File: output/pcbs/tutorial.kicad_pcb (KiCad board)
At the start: 2 copper layers, 379.6 x 123.2 mm, 184 parts

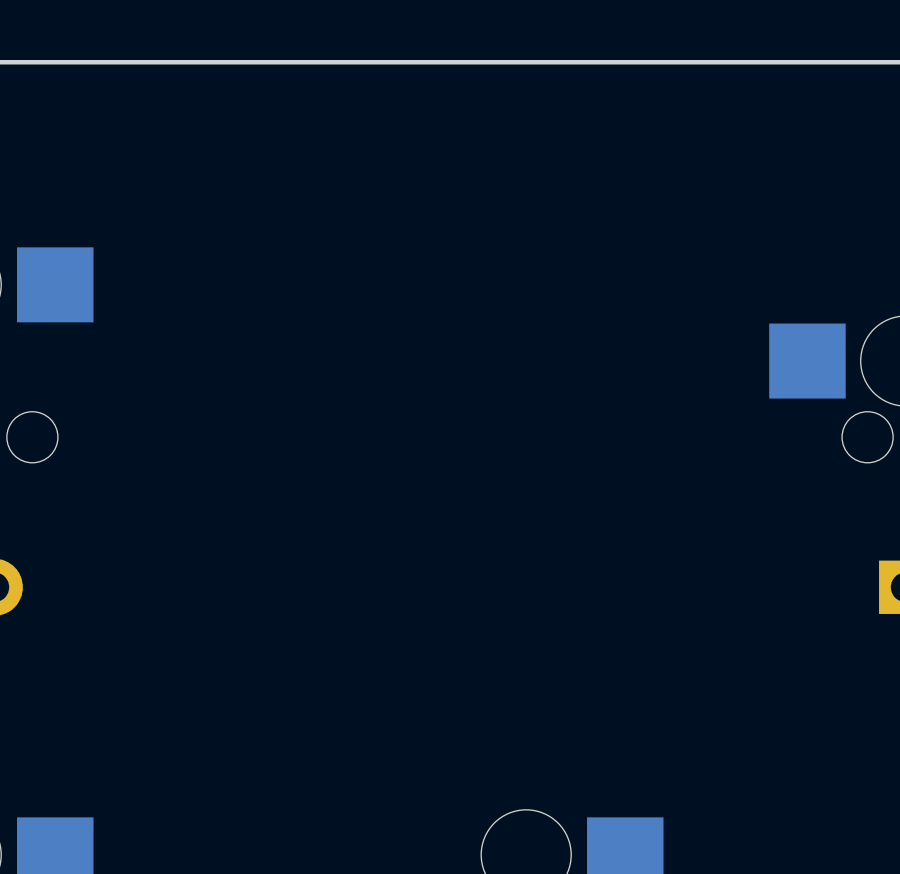
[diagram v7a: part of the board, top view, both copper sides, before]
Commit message: added dip-16
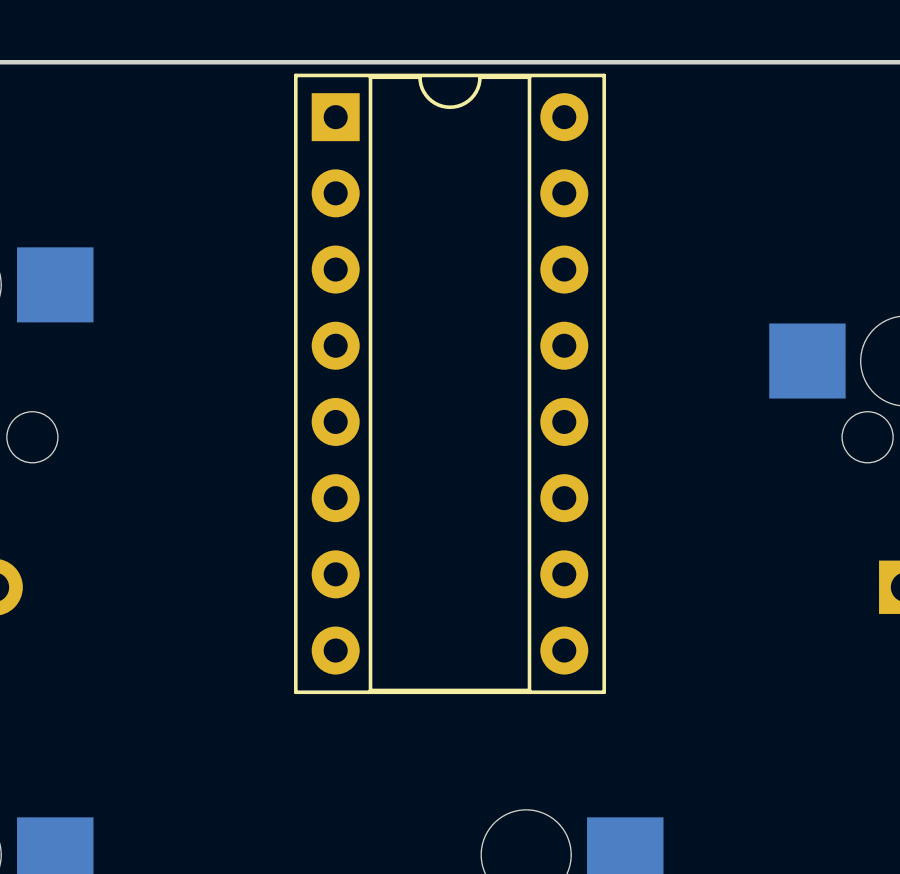
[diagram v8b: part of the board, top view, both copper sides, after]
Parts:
- added DIP1: DIP-16_W7.62mm_Socket, DIP-16_W7.62mm_Socket, F.Cu at (42.2, 69.3)
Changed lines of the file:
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@@
         (pad 24 thru_hole circle (at 13.97 -7.62 0) (size 1.7526 1.7526) (drill 1.0922) (layers *.Cu *.SilkS *.Mask) (net 72 "P9"))
       )
+    (module DIP-16_W7.62mm_Socket (layer F.Cu)
+  (descr "16-lead though-hole mounted DIP package, row spacing 7.62 mm (300 mils), Socket")
+  (at 42.19 69.33 0)
+  (tags "THT DIP DIL PDIP 2.54mm 7.62mm 300mil Socket")
+  (fp_text reference "DIP1" (at 3.81 -2.33) (layer F.SilkS) hide
+    (effects (font (size 1 1) (thickness 0.15)))
+  )
+  (fp_text value DIP-16_W7.62mm_Socket (at 3.81 20.11) (layer F.Fab)
+    (effects (font (size 1 1) (thickness 0.15)))
+  )
+  (fp_arc (start 3.81 -1.33) (end 2.81 -1.33) (angle -180.000000) (layer F.SilkS) (width 0.12))
+  (fp_line (start 1.635 -1.27) (end 6.985 -1.27) (layer F.Fab) (width 0.1))
+  (fp_line (start 6.985 -1.27) (end 6.985 19.05) (layer F.Fab) (width 0.1))
+  (fp_line (start 6.985 19.05) (end 0.635 19.05) (layer F.Fab) (width 0.1))
+  (fp_line (start 0.635 19.05) (end 0.635 -0.27) (layer F.Fab) (width 0.1))
+  (fp_line (start 0.635 -0.27) (end 1.635 -1.27) (layer F.Fab) (width 0.1))
+  (fp_line (start -1.27 -1.33) (end -1.27 19.11) (layer F.Fab) (width 0.1))
+  (fp_line (start -1.27 19.11) (end 8.89 19.11) (layer F.Fab) (width 0.1))
+  (fp_line (start 8.89 19.11) (end 8.89 -1.33) (layer F.Fab) (width 0.1))
+  (fp_line (start 8.89 -1.33) (end -1.27 -1.33) (layer F.Fab) (width 0.1))
+  (fp_line (start 2.81 -1.33) (end 1.16 -1.33) (layer F.SilkS) (width 0.12))
+  (fp_line (start 1.16 -1.33) (end 1.16 19.11) (layer F.SilkS) (width 0.12))
+  (fp_line (start 1.16 19.11) (end 6.46 19.11) (layer F.SilkS) (width 0.12))
+  (fp_line (start 6.46 19.11) (end 6.46 -1.33) (layer F.SilkS) (width 0.12))
+  (fp_line (start 6.46 -1.33) (end 4.81 -1.33) (layer F.SilkS) (width 0.12))
+  (fp_line (start -1.33 -1.39) (end -1.33 19.17) (layer F.SilkS) (width 0.12))
+  (fp_line (start -1.33 19.17) (end 8.95 19.17) (layer F.SilkS) (width 0.12))
+  (fp_line (start 8.95 19.17) (end 8.95 -1.39) (layer F.SilkS) (width 0.12))
+  (fp_line (start 8.95 -1.39) (end -1.33 -1.39) (layer F.SilkS) (width 0.12))
+  (fp_line (start -1.55 -1.6) (end -1.55 19.4) (layer F.CrtYd) (width 0.05))
+  (fp_line (start -1.55 19.4) (end 9.15 19.4) (layer F.CrtYd) (width 0.05))
+  (fp_line (start 9.15 19.4) (end 9.15 -1.6) (layer F.CrtYd) (width 0.05))
+  (fp_line (start 9.15 -1.6) (end -1.55 -1.6) (layer F.CrtYd) (width 0.05))
+  (pad 1 thru_hole rect (at 0 0) (size 1.6 1.6) (drill 0.8) (layers *.Cu *.Mask) (net 52 "GND"))
+  (pad 9 thru_hole oval (at 7.62 17.78) (size 1.6 1.6) (drill 0.8) (layers *.Cu *.Mask) (net 52 "GND"))
+  (pad 2 thru_hole oval (at 0 2.54) (size 1.6 1.6) (drill 0.8) (layers *.Cu *.Mask) (net 52 "GND"))
+  (pad 10 thru_hole oval (at 7.62 15.24) (size 1.6 1.6) (drill 0.8) (layers *.Cu *.Mask) (net 52 "GND"))
+  (pad 3 thru_hole oval (at 0 5.08) (size 1.6 1.6) (drill 0.8) (layers *.Cu *.Mask) (net 52 "GND"))
+  (pad 11 thru_hole oval (at 7.62 12.7) (size 1.6 1.6) (drill 0.8) (layers *.Cu *.Mask) (net 52 "GND"))
+  (pad 4 thru_hole oval (at 0 7.62) (size 1.6 1.6) (drill 0.8) (layers *.Cu *.Mask) (net 52 "GND"))
+  (pad 12 thru_hole oval (at 7.62 10.16) (size 1.6 1.6) (drill 0.8) (layers *.Cu *.Mask) (net 52 "GND"))
+  (pad 5 thru_hole oval (at 0 10.16) (size 1.6 1.6) (drill 0.8) (layers *.Cu *.Mask) (net 52 "GND"))
+  (pad 13 thru_hole oval (at 7.62 7.62) (size 1.6 1.6) (drill 0.8) (layers *.Cu *.Mask) (net 52 "GND"))
+  (pad 6 thru_hole oval (at 0 12.7) (size 1.6 1.6) (drill 0.8) (layers *.Cu *.Mask) (net 52 "GND"))
+  (pad 14 thru_hole oval (at 7.62 5.08) (size 1.6 1.6) (drill 0.8) (layers *.Cu *.Mask) (net 52 "GND"))
+  (pad 7 thru_hole oval (at 0 15.24) (size 1.6 1.6) (drill 0.8) (layers *.Cu *.Mask) (net 52 "GND"))
+  (pad 15 thru_hole oval (at 7.62 2.54) (size 1.6 1.6) (drill 0.8) (layers *.Cu *.Mask) (net 52 "GND"))
+  (pad 8 thru_hole oval (at 0 17.78) (size 1.6 1.6) (drill 0.8) (layers *.Cu *.Mask) (net 52 "GND"))
+  (pad 16 thru_hole oval (at 7.62 0) (size 1.6 1.6) (drill 0.8) (layers *.Cu *.Mask) (net 54 "VCC"))
+  (fp_text user %R (at 3.81 8.89) (layer F.Fab)
+    (effects (font (size 1 1) (thickness 0.15)))
+  )
+  (model /Package_DIP.3dshapes/DIP-16_W7.62mm_Socket.wrl
+    (at (xyz 0 0 0))
+    (scale (xyz 1 1 1))
+    (rotate (xyz 0 0 0))
+  )
+)
     (module E73:SW_TACT_ALPS_SKQGABE010 (layer F.Cu)
         (descr "Low-profile SMD Tactile Switch, https://www.e-switch.com/product-catalog/tact/product-lines/tl3342-series-low-profile-smt-tact-switch")
